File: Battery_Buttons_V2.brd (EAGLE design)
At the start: 17.8 x 35.6 mm, 9 parts

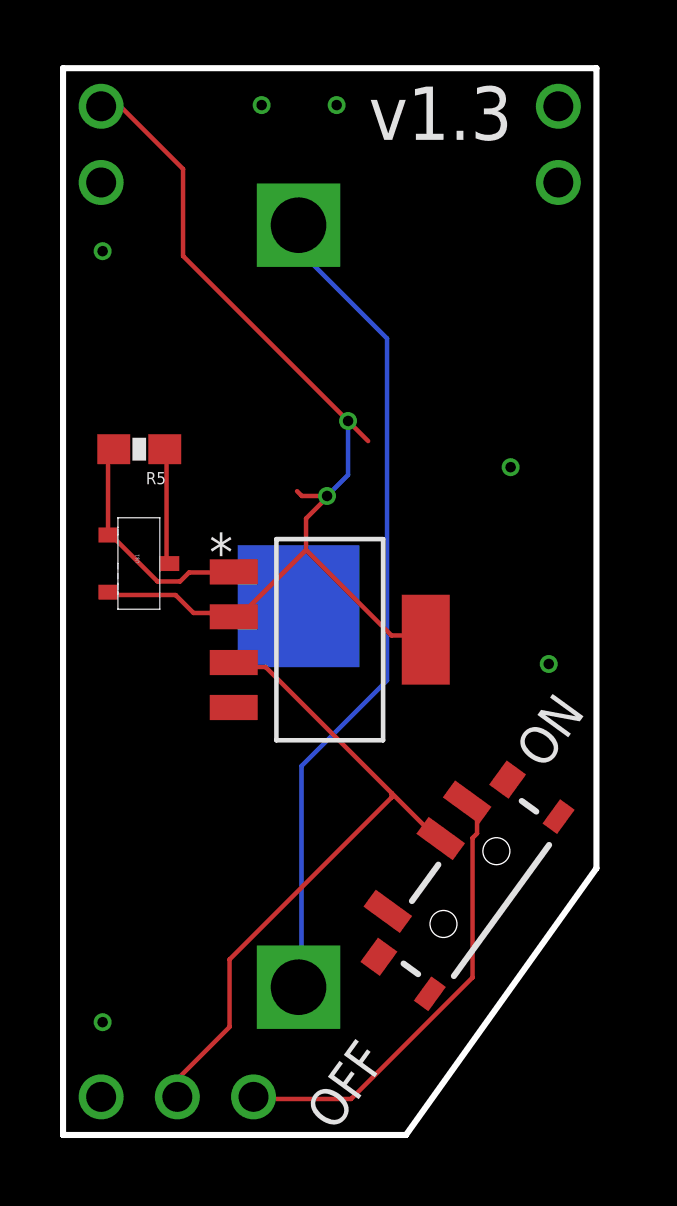
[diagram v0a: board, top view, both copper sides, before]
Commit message: created new Battery package and added it to the PCB. I have also moved the switch around. Need to check for DRC errors etc
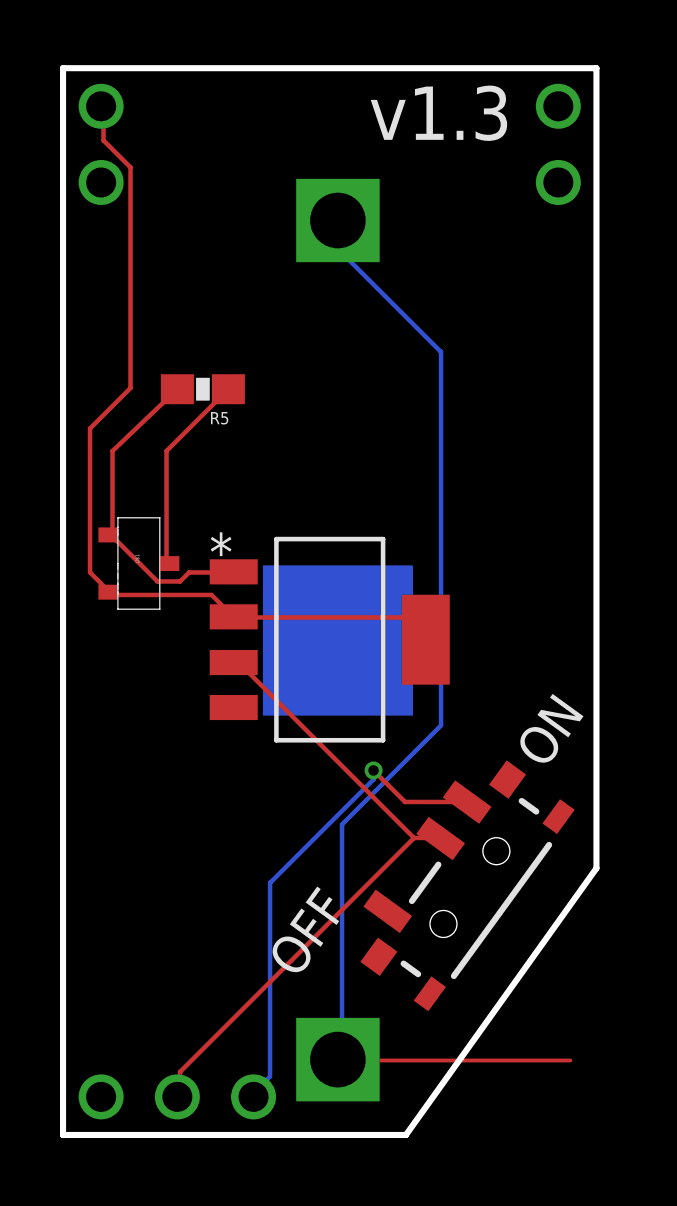
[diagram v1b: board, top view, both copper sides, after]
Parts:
- BAT1: device SparkFun-Electromechanical:BATTCON_245MM_PTH -> STM1061:BATTCON_245MM_PTH
- moved R5 2.92 mm to (4.66, 24.9)
- moved BAT1 1.74 mm to (9.16, 16.5)
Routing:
- net GND: track 34.4 -> 28.7 mm, vias 2 -> 0
- net VBAT: track 27.9 -> 30.9 mm
- net N$4: track 7.88 -> 10.8 mm
- net N$11: track 3.94 -> 6.77 mm
- net N$1: track 22.5 -> 21.3 mm
- net N$5: track 15.0 -> 16.1 mm, vias 0 -> 1
